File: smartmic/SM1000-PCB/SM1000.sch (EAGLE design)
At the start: 153 parts, among them CN1 HDR100-6, CN2 MOLEX-MINI-B-SMT, CN3 RASM712PX, CN4 RJ-45, CN5 MJ-3523-SMT, CN6 MJ-3523-SMT, CN7 MJ-3523-SMT, CN8 MJ-3523-SMT, CN9 MJ-3523-SMT, IC1 DIL-16, J1 JMP-2PIN, J2 JMP-2PIN, J3 JMP-2PIN, J5 JMPR-3PIN, Q1 MMBT4401, Q2 MMBT4401, SW2 SW-SPST-2-1437565-0, SW3 DPDT, T1 SM-LP-5001, T2 SM-LP-5001, U1 STM32F407, U2 LD3985M33R, U3 STMPS2141, U4 EMIF02-USB03F2, U5 TPS54329E, U6 LMV341, U7 LMV341, U8 LM386M-1, X1 8.0MHz

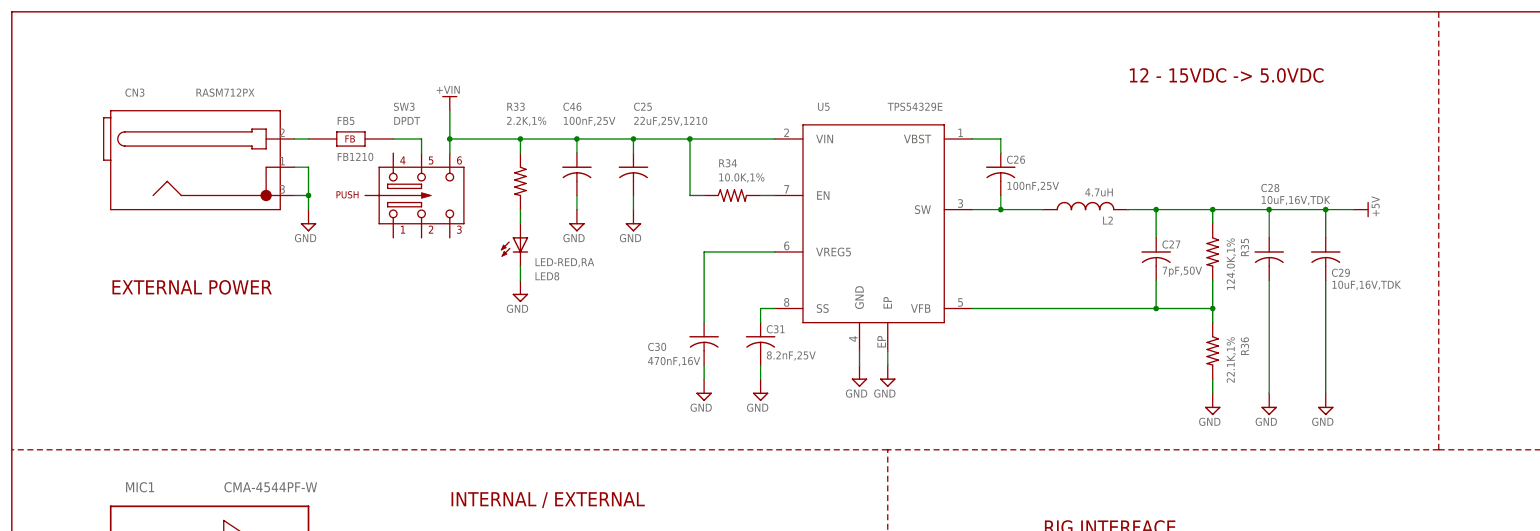
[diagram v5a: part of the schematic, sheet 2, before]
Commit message: Add polarity protection. Add 47Ohm resistor to VREF+ circuit Continue PCB layout
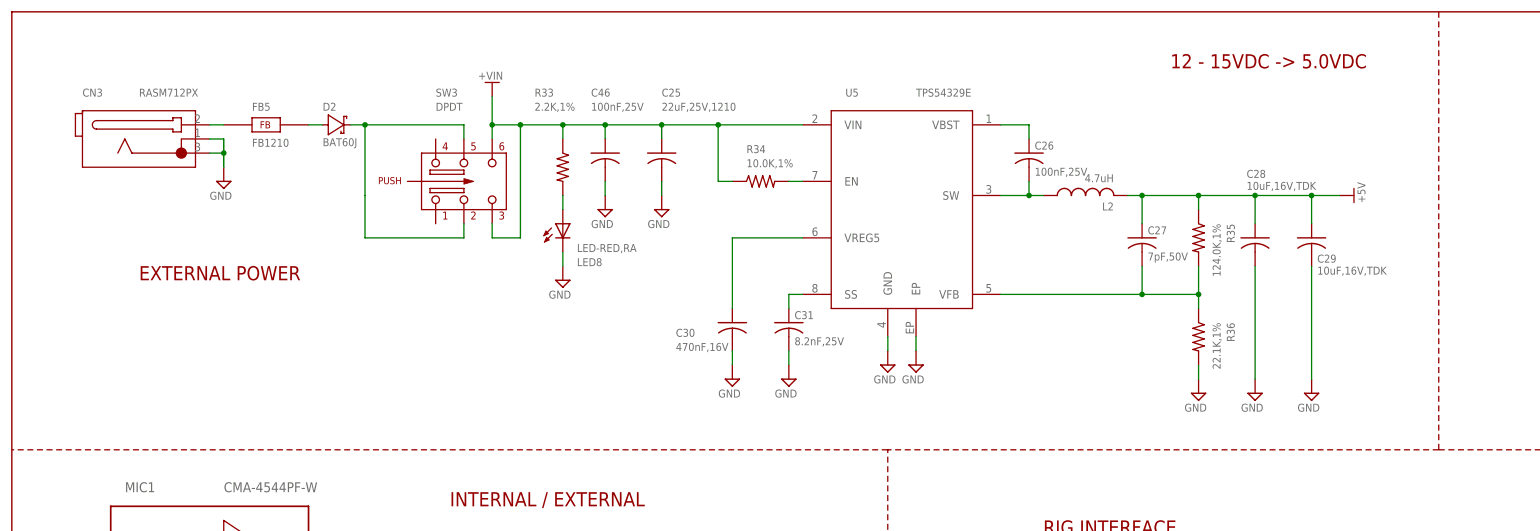
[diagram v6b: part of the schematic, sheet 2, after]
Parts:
- added D2: BAT60J, _RoweTel:BAT60J
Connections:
- net N$24 renamed SW
- removed net N$78: FB5.2, SW3.5
- new net N$24: D2.A, FB5.2
- new net N$80: D2.C, SW3.2, SW3.5
- net +VIN: now also SW3.3
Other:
- moved on the sheet: C25, C26, C27, C28, C29, C30, C31, C46, FB5, L2, LED8, R33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

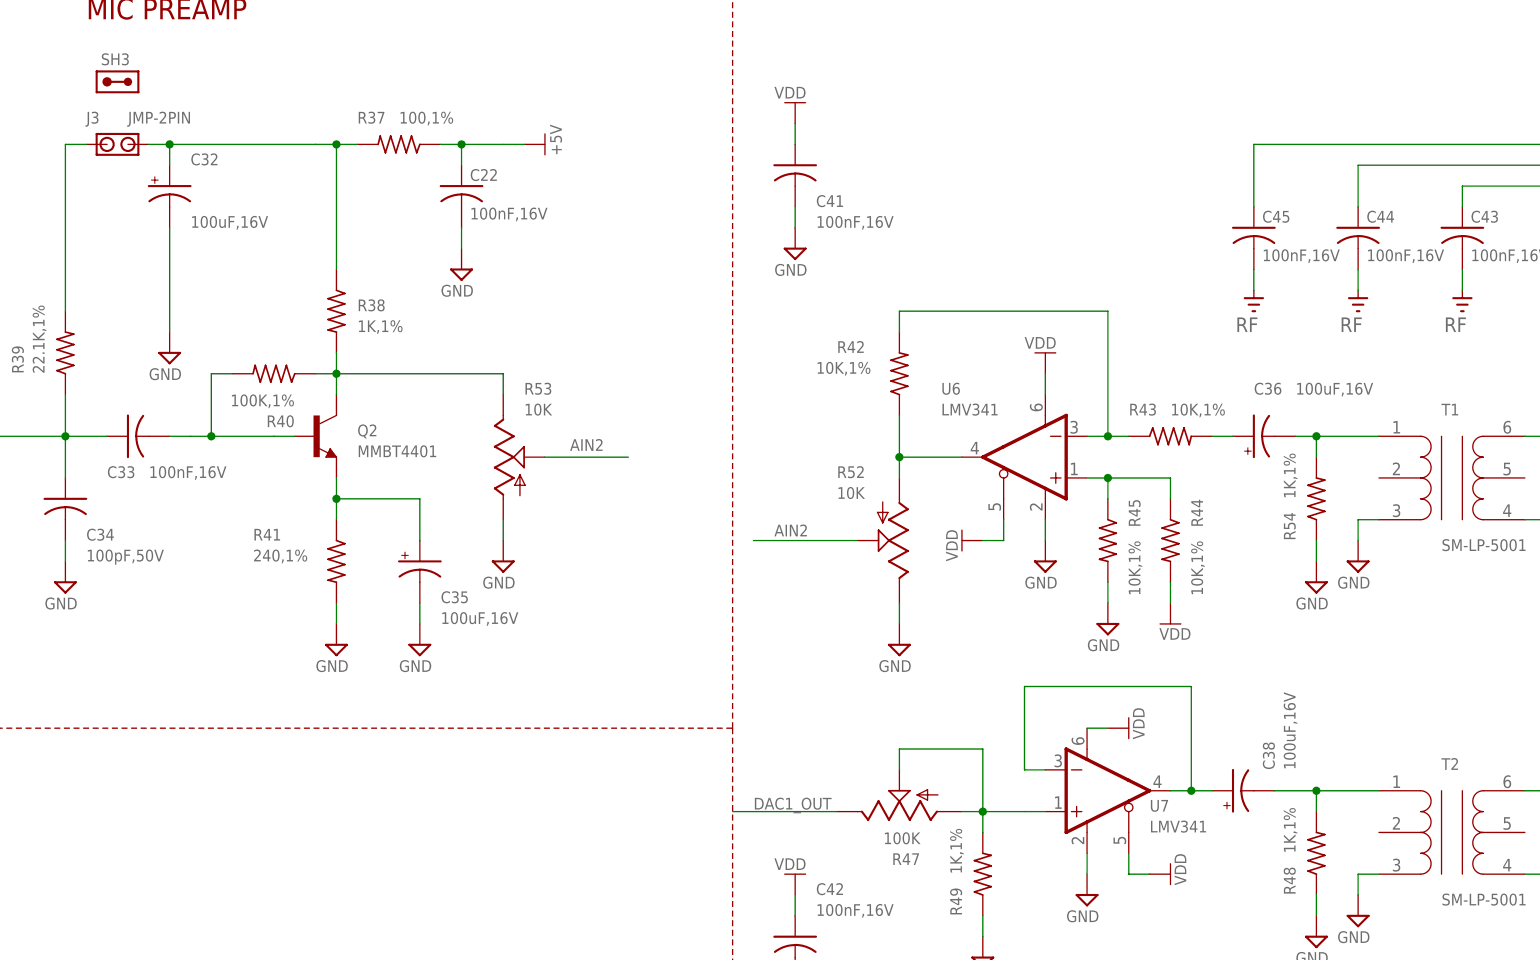
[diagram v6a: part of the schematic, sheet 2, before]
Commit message: Change large electrolytic caps to ceramic for space reasons.
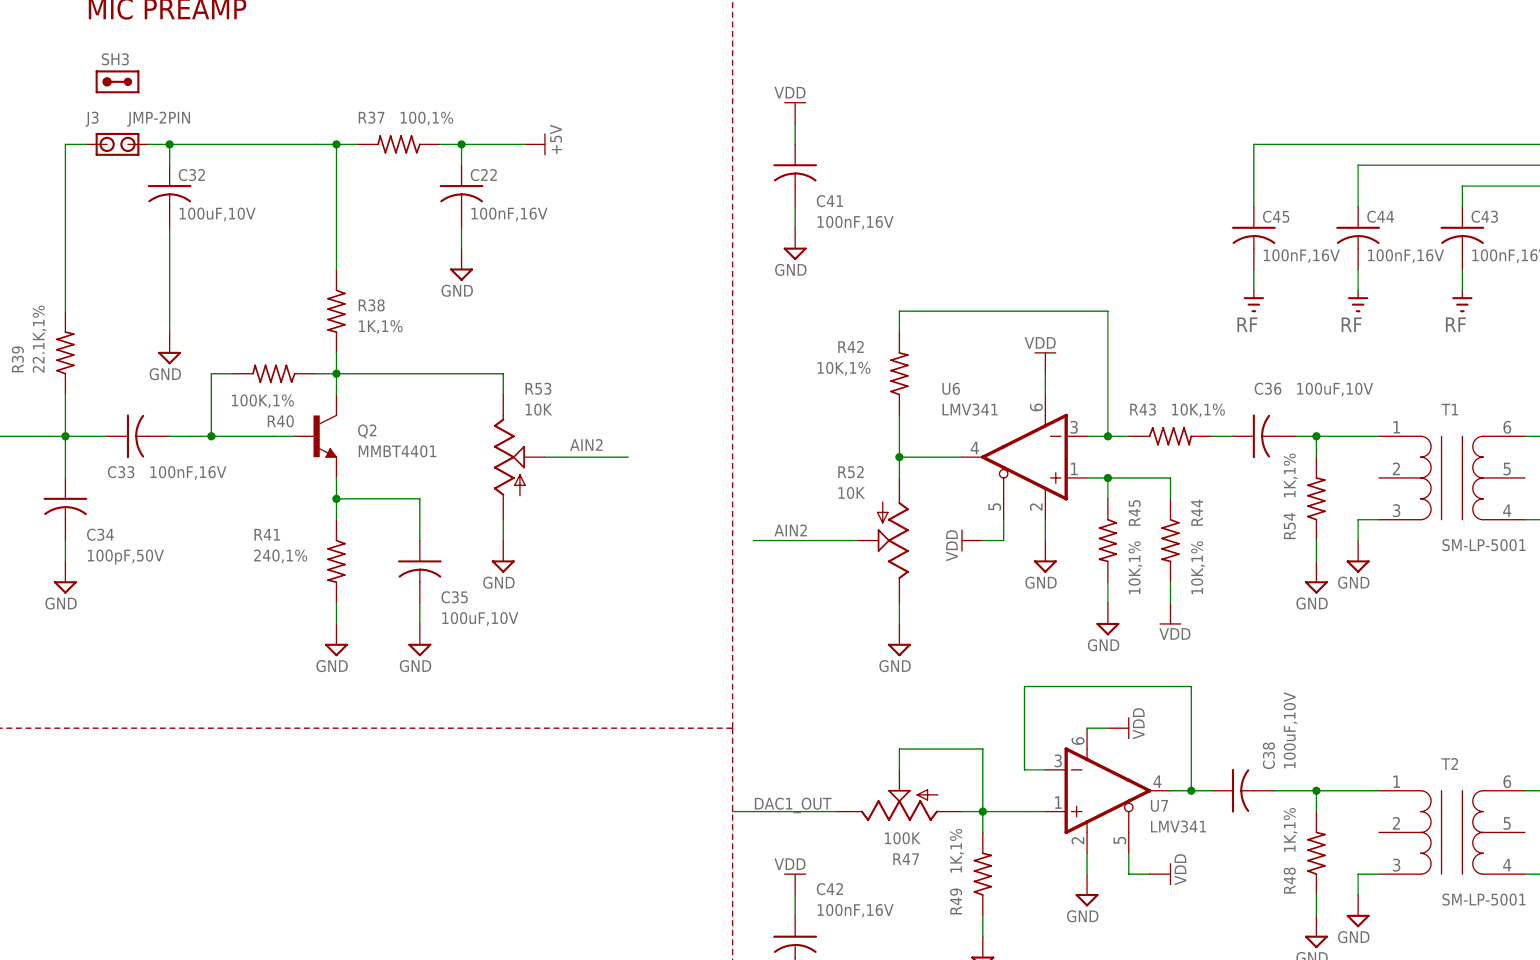
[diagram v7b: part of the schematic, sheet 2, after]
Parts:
- C32, C35, C36, C38: value 100uF,16V -> 100uF,10V; device _RoweTel:CAP-CHEMI-MVE-F55 -> SM1000:CAP-1210
- CN2: device _RoweTel:MOLEX-MINI-B-SMT -> SM1000:MOLEX-MINI-B-SMT
- LD1: device _RoweTel:LED-R/G -> SM1000:LED-R/G
- U1: device _RoweTel:STM32F407 -> SM1000:STM32F407
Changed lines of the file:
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@@
 <part name="V36" library="A-SUPPLY2" deviceset="VDD" device=""/>
 <part name="SH2" library="_Coherix" deviceset="SHUNT,0.1IN" device=""/>
-<part name="LD1" library="_RoweTel" deviceset="LED-R/G" device=""/>
+<part name="LD1" library="SM1000" deviceset="LED-R/G" device=""/>
 <part name="V37" library="A-SUPPLY2" deviceset="GND" device=""/>
 <part name="R3" library="_Coherix" deviceset="RES0603" device="" value="1K,1%"/>
@@
 <part name="C34" library="_RoweTel" deviceset="CAP-0603" device="" value="100pF,50V"/>
 <part name="R39" library="_RoweTel" deviceset="RES0603" device="" value="22.1K,1%"/>
-<part name="C32" library="_RoweTel" deviceset="CAP-CHEMI-MVE-F55" device="" value="100uF,16V"/>
+<part name="C32" library="SM1000" deviceset="CAP-1210" device="" value="100uF,10V"/>
 <part name="Q2" library="_RoweTel" deviceset="MMBT4401" device=""/>
 <part name="R40" library="_RoweTel" deviceset="RES0603" device="" value="100K,1%"/>
 <part name="R41" library="_RoweTel" deviceset="RES0603" device="" value="240,1%"/>
-<part name="C35" library="_RoweTel" deviceset="CAP-CHEMI-MVE-F55" device="" value="100uF,16V"/>
+<part name="C35" library="SM1000" deviceset="CAP-1210" device="" value="100uF,10V"/>
 <part name="V59" library="A-SUPPLY2" deviceset="GND" device=""/>
 <part name="V60" library="A-SUPPLY2" deviceset="GND" device=""/>
@@
 <part name="V78" library="A-SUPPLY2" deviceset="GND" device=""/>
 <part name="V79" library="A-SUPPLY2" deviceset="GND" device=""/>
-<part name="U1" library="_RoweTel" deviceset="STM32F407" device=""/>
+<part name="U1" library="SM1000" deviceset="STM32F407" device=""/>
 <part name="V80" library="A-SUPPLY2" deviceset="RF" device=""/>
 <part name="CN4" library="_Coherix" deviceset="CONN-RJ45-MOLEX-44144-003" device="" value="RJ-45"/>
@@
 <part name="V86" library="A-SUPPLY2" deviceset="VDD" device=""/>
 <part name="V88" library="A-SUPPLY2" deviceset="VDD" device=""/>
-<part name="C38" library="_RoweTel" deviceset="CAP-CHEMI-MVE-F55" device="" value="100uF,16V"/>
+<part name="C38" library="SM1000" deviceset="CAP-1210" device="" value="100uF,10V"/>
 <part name="R48" library="_RoweTel" deviceset="RES0603" device="" value="1K,1%"/>
 <part name="V87" library="A-SUPPLY2" deviceset="GND" device=""/>
 <part name="R49" library="_RoweTel" deviceset="RES0603" device="" value="1K,1%"/>
 <part name="V89" library="A-SUPPLY2" deviceset="GND" device=""/>
-<part name="C36" library="_RoweTel" deviceset="CAP-CHEMI-MVE-F55" device="" value="100uF,16V"/>
+<part name="C36" library="SM1000" deviceset="CAP-1210" device="" value="100uF,10V"/>
 <part name="B-FRAME3" library="_RoweTel" deviceset="GENERICL-B-SIZE" device=""/>
 <part name="B-FRAME2" library="_RoweTel" deviceset="GENERICL-B-SIZE" device=""/>
-<part name="CN2" library="_RoweTel" deviceset="MOLEX-MINI-B-SMT" device=""/>
+<part name="CN2" library="SM1000" deviceset="MOLEX-MINI-B-SMT" device=""/>
 <part name="PCB1" library="_Coherix" deviceset="PCB" device="" value="SM1000A"/>
 <part name="U$7" library="A-SUPPLY2" deviceset="+VIN" device=""/>

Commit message: Try commit again.
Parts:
- C23: value 100nF,16V -> 100nF,25V
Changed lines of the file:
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@@
 <parts>
 <part name="U4" library="AA-IC" deviceset="EMIF02-USB03F2" device=""/>
-<part name="MIC1" library="_RoweTel" deviceset="CMA-4544PF-W" device=""/>
 <part name="CN5" library="_RoweTel" deviceset="MJ-3523-SMT" device=""/>
 <part name="CN8" library="_RoweTel" deviceset="MJ-3523-SMT" device=""/>
@@
 <part name="V93" library="A-SUPPLY2" deviceset="GND" device=""/>
 <part name="C22" library="_RoweTel" deviceset="CAP-0603" device="" value="100nF,16V"/>
-<part name="C23" library="_RoweTel" deviceset="CAP-0603" device="" value="100nF,16V"/>
+<part name="C23" library="_RoweTel" deviceset="CAP-0603" device="" value="100nF,25V"/>
 <part name="C41" library="_RoweTel" deviceset="CAP-0603" device="" value="100nF,16V"/>
 <part name="C42" library="_RoweTel" deviceset="CAP-0603" device="" value="100nF,16V"/>
@@
 <part name="R10" library="_Coherix" deviceset="RES0603" device="" value="47,1%"/>
 <part name="D2" library="_RoweTel" deviceset="BAT60J" device=""/>
+<part name="MIC1" library="_RoweTel" deviceset="CMA-4544PF-W" device=""/>
 </parts>
 <sheets>
@@
 </plain>
 <instances>
-<instance part="MIC1" gate="G$1" x="38.1" y="172.72"/>
 <instance part="CN5" gate="G$1" x="33.02" y="129.54" rot="MR180"/>
 <instance part="CN8" gate="G$1" x="119.38" y="53.34" rot="R180"/>
@@
 <instance part="V102" gate="GND" x="106.68" y="243.84"/>
 <instance part="D2" gate="G$1" x="58.42" y="259.08" rot="R180"/>
+<instance part="MIC1" gate="G$1" x="38.1" y="172.72"/>
 </instances>
 <busses>
@@
 </segment>
 <segment>
-<pinref part="MIC1" gate="G$1" pin="2"/>
 <pinref part="V55" gate="GND" pin="GND"/>
 <wire x1="58.42" y1="165.1" x2="60.96" y2="165.1" width="0.1524" layer="91"/>
 <wire x1="60.96" y1="165.1" x2="60.96" y2="162.56" width="0.1524" layer="91"/>
+<pinref part="MIC1" gate="G$1" pin="2"/>
 </segment>
 <segment>
@@
 <net name="N$32" class="0">
 <segment>
-<pinref part="MIC1" gate="G$1" pin="1"/>
 <wire x1="58.42" y1="182.88" x2="66.04" y2="182.88" width="0.1524" layer="91"/>
 <wire x1="66.04" y1="182.88" x2="66.04" y2="149.86" width="0.1524" layer="91"/>
 <pinref part="J5" gate="G$1" pin="1"/>
 <wire x1="66.04" y1="149.86" x2="53.34" y2="149.86" width="0.1524" layer="91"/>
-</segment>
-</net>
+<pinref part="MIC1" gate="G$1" pin="1"/>
+</segment>
+</net>
